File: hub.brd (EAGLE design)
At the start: 160 x 100 mm, 33 parts, among them U1 10118194-MICRO-USB, U2 LM3671MF-3.3/NOPBMF05A-M, U3 SN74LVC1T45DBVRDBV6-M, U4 SN74LVC1T45DBVRDBV6-M

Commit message: First draft complete?
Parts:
- removed JP3: I2C, pinhead:1X04
- removed LED2, LED3: (no value), led:CHIPLED_0805
- removed R7, R8: (no value), rcl:R0805
- removed U$7, U$8: KMR641NG, nebrius:KMR641NG
- added U$5: SSD1306-OLED, nebrius:SSD1306-OLED
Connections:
- removed net IO34: JP7.7, U$2.6
- removed net IO35: JP7.9, U$2.7
- removed net IO36: JP7.3, U$2.4
- removed net IO39: JP7.5, U$2.5
- removed net N$11: LED2.C, R7.2
- removed net N$13: LED3.C, R8.2
- removed net N$14: LED3.A, U$2.31
- removed net N$15: LED2.A, U$2.29
- new net IO19: JP7.2, U$2.31
- new net IO27: JP7.9, U$2.12
- new net IO33: JP7.3, U$2.9
- new net IO4: JP7.8, U$2.26
- net EN: no longer U$7.P$3
- net GND: now also U$5.2; no longer JP3.1, R7.1, R8.1, U$7.P$1, U$8.P$1
- net IO0: no longer U$8.P$3
- net IO16: now also JP7.4; no longer JP7.8
- net IO25: now also JP7.5; no longer JP7.2
- net IO26: now also JP7.7; no longer JP7.4
- net SCL: now also U$5.3; no longer JP3.4
- net SDA: now also U$5.4; no longer JP3.3
- net VCC: now also U$5.1; no longer JP3.2

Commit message: Polishing
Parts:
- R6: value 68 -> 220
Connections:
- net IO16 renamed GPIO16
- removed net IO17: JP7.6, U$2.28
- removed net IO19: JP7.2, U$2.31
- removed net IO25: JP7.5, U$2.10
- removed net IO26: JP7.7, U$2.11
- removed net IO27: JP7.9, U$2.12
- removed net IO33: JP7.3, U$2.9
- removed net IO4: JP7.8, U$2.26
- new net GPIO17: JP7.2, U$2.28
- new net GPIO25: JP7.7, U$2.10
- new net GPIO26: JP7.9, U$2.11
- new net GPIO27: JP7.8, U$2.12
- new net GPIO32: JP7.3, U$2.8
- new net GPIO33: JP7.5, U$2.9
- new net GPIO4: JP7.6, U$2.26
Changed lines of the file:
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@@
 <attribute name="VALUE" x="-82.296" y="-39.878" size="1.27" layer="27" ratio="10"/>
 </element>
-<element name="R6" library="rcl" library_urn="urn:adsk.eagle:library:334" package="R0805" package3d_urn="urn:adsk.eagle:package:23553/2" value="68" x="-80.01" y="-44.45" smashed="yes">
+<element name="R6" library="rcl" library_urn="urn:adsk.eagle:library:334" package="R0805" package3d_urn="urn:adsk.eagle:package:23553/2" value="220" x="-80.01" y="-44.45" smashed="yes">
 <attribute name="NAME" x="-80.645" y="-43.18" size="1.27" layer="25"/>
 <attribute name="POPULARITY" value="85" x="-80.01" y="-44.45" size="1.778" layer="27" display="off"/>
@@
 <wire x1="-79.06" y1="-44.45" x2="-86.36" y2="-42.13" width="0" layer="19" extent="1-1"/>
 </signal>
-<signal name="IO17">
-<contactref element="U$2" pad="28"/>
-<contactref element="JP7" pad="6"/>
-<wire x1="-104.53" y1="-48.26" x2="-115.57" y2="-60.96" width="0" layer="19" extent="1-1"/>
-</signal>
-<signal name="IO16">
+<signal name="GPIO16">
 <contactref element="U$2" pad="27"/>
 <contactref element="JP7" pad="4"/>
 <wire x1="-104.53" y1="-49.53" x2="-118.11" y2="-60.96" width="0" layer="19" extent="1-1"/>
 </signal>
-<signal name="IO25">
+<signal name="GPIO33">
+<contactref element="U$2" pad="9"/>
+<contactref element="JP7" pad="5"/>
+<wire x1="-121.53" y1="-45.72" x2="-115.57" y2="-63.5" width="0" layer="19" extent="1-1"/>
+</signal>
+<signal name="GPIO27">
+<contactref element="U$2" pad="12"/>
+<contactref element="JP7" pad="8"/>
+<wire x1="-121.53" y1="-49.53" x2="-113.03" y2="-60.96" width="0" layer="19" extent="1-1"/>
+</signal>
+<signal name="GPIO4">
+<contactref element="U$2" pad="26"/>
+<contactref element="JP7" pad="6"/>
+<wire x1="-104.53" y1="-50.8" x2="-115.57" y2="-60.96" width="0" layer="19" extent="1-1"/>
+</signal>
+<signal name="GPIO32">
+<contactref element="U$2" pad="8"/>
+<contactref element="JP7" pad="3"/>
+<wire x1="-121.53" y1="-44.45" x2="-118.11" y2="-63.5" width="0" layer="19" extent="1-1"/>
+</signal>
+<signal name="GPIO25">
 <contactref element="U$2" pad="10"/>
-<contactref element="JP7" pad="5"/>
-<wire x1="-121.53" y1="-46.99" x2="-115.57" y2="-63.5" width="0" layer="19" extent="1-1"/>
-</signal>
-<signal name="IO26">
+<contactref element="JP7" pad="7"/>
+<wire x1="-121.53" y1="-46.99" x2="-113.03" y2="-63.5" width="0" layer="19" extent="1-1"/>
+</signal>
+<signal name="GPIO26">
 <contactref element="U$2" pad="11"/>
-<contactref element="JP7" pad="7"/>
-<wire x1="-121.53" y1="-48.26" x2="-113.03" y2="-63.5" width="0" layer="19" extent="1-1"/>
-</signal>
-<signal name="IO33">
-<contactref element="U$2" pad="9"/>
-<contactref element="JP7" pad="3"/>
-<wire x1="-121.53" y1="-45.72" x2="-118.11" y2="-63.5" width="0" layer="19" extent="1-1"/>
-</signal>
-<signal name="IO27">
-<contactref element="U$2" pad="12"/>
 <contactref element="JP7" pad="9"/>
-<wire x1="-121.53" y1="-49.53" x2="-110.49" y2="-63.5" width="0" layer="19" extent="1-1"/>
-</signal>
-<signal name="IO4">
-<contactref element="U$2" pad="26"/>
-<contactref element="JP7" pad="8"/>
-<wire x1="-104.53" y1="-50.8" x2="-113.03" y2="-60.96" width="0" layer="19" extent="1-1"/>
-</signal>
-<signal name="IO19">
-<contactref element="U$2" pad="31"/>
+<wire x1="-121.53" y1="-48.26" x2="-110.49" y2="-63.5" width="0" layer="19" extent="1-1"/>
+</signal>
+<signal name="GPIO17">
+<contactref element="U$2" pad="28"/>
 <contactref element="JP7" pad="2"/>
-<wire x1="-104.53" y1="-44.45" x2="-120.65" y2="-60.96" width="0" layer="19" extent="1-1"/>
+<wire x1="-104.53" y1="-48.26" x2="-120.65" y2="-60.96" width="0" layer="19" extent="1-1"/>
 </signal>
 </signals>

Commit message: Tweaked and confirmed some connections
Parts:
- removed JP5: LED Type, jumper:JP2
- removed JP6: JTAG Enable, jumper:JP2
- added JP3: JTAG, pinhead:2X03
- JP1: value JTAG -> 3-pin LED strip; device pinhead:1X06 -> pinhead:1X03/90
- JP4: value LED Strip -> 4-pin LED Strip
- moved U$5 254.1 mm to (99.1, 54.6)
- moved JP7 245.7 mm to (102.9, 50.2)
- moved U$2 242.1 mm to (99.1, 81.3)
- moved JP4 197.7 mm to (118.7, 54.6), turned to 180 degrees
- moved JP1 187.1 mm to (117.5, 50.8), turned to 180 degrees
- moved S1 167.2 mm to (117.5, 67.9)
- moved U$3 151.1 mm to (85.1, 76.2), turned to 270 degrees
- moved U1 120.8 mm to (80.6, 64.8), turned to 270 degrees
- moved JP2 108.6 mm to (87.0, 51.4), turned to 180 degrees
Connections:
- removed net N$7: JP4.3, JP5.2
- removed net TRST_N: JP1.1, JP6.1
- net EN: now also JP3.1; no longer JP6.2, JP6.3
- net GND: now also JP1.1, JP3.6; no longer JP1.6, JP5.1
- net N$8: now also JP1.2, JP4.3; no longer JP4.2
- net N$9: now also JP4.2; no longer JP5.3
- net TCK: now also JP3.4; no longer JP1.4
- net TDI: now also JP3.3; no longer JP1.3
- net TDO: now also JP3.2; no longer JP1.2
- net TMS: now also JP3.5; no longer JP1.5
- net VCC: now also JP1.3

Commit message: More component arrangement
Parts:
- JP7: value (none) -> GPIO
- moved U$3 5.08 mm to (85.1, 71.1)
- moved U1 5.08 mm to (80.6, 59.7)
- moved JP3 0.64 mm to (118.1, 78.1), turned to 90 degrees
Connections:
- net GND: now also U1.M1, U1.M2, U1.M3, U1.M4
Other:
- outline, holes or cut-outs redrawn
- board text added: "EN"
- board text added: "GND"
- board text added: "Off"
- board text added: "TCK"
- board text added: "TDI"
- board text added: "TDO"
- board text added: "TMS"

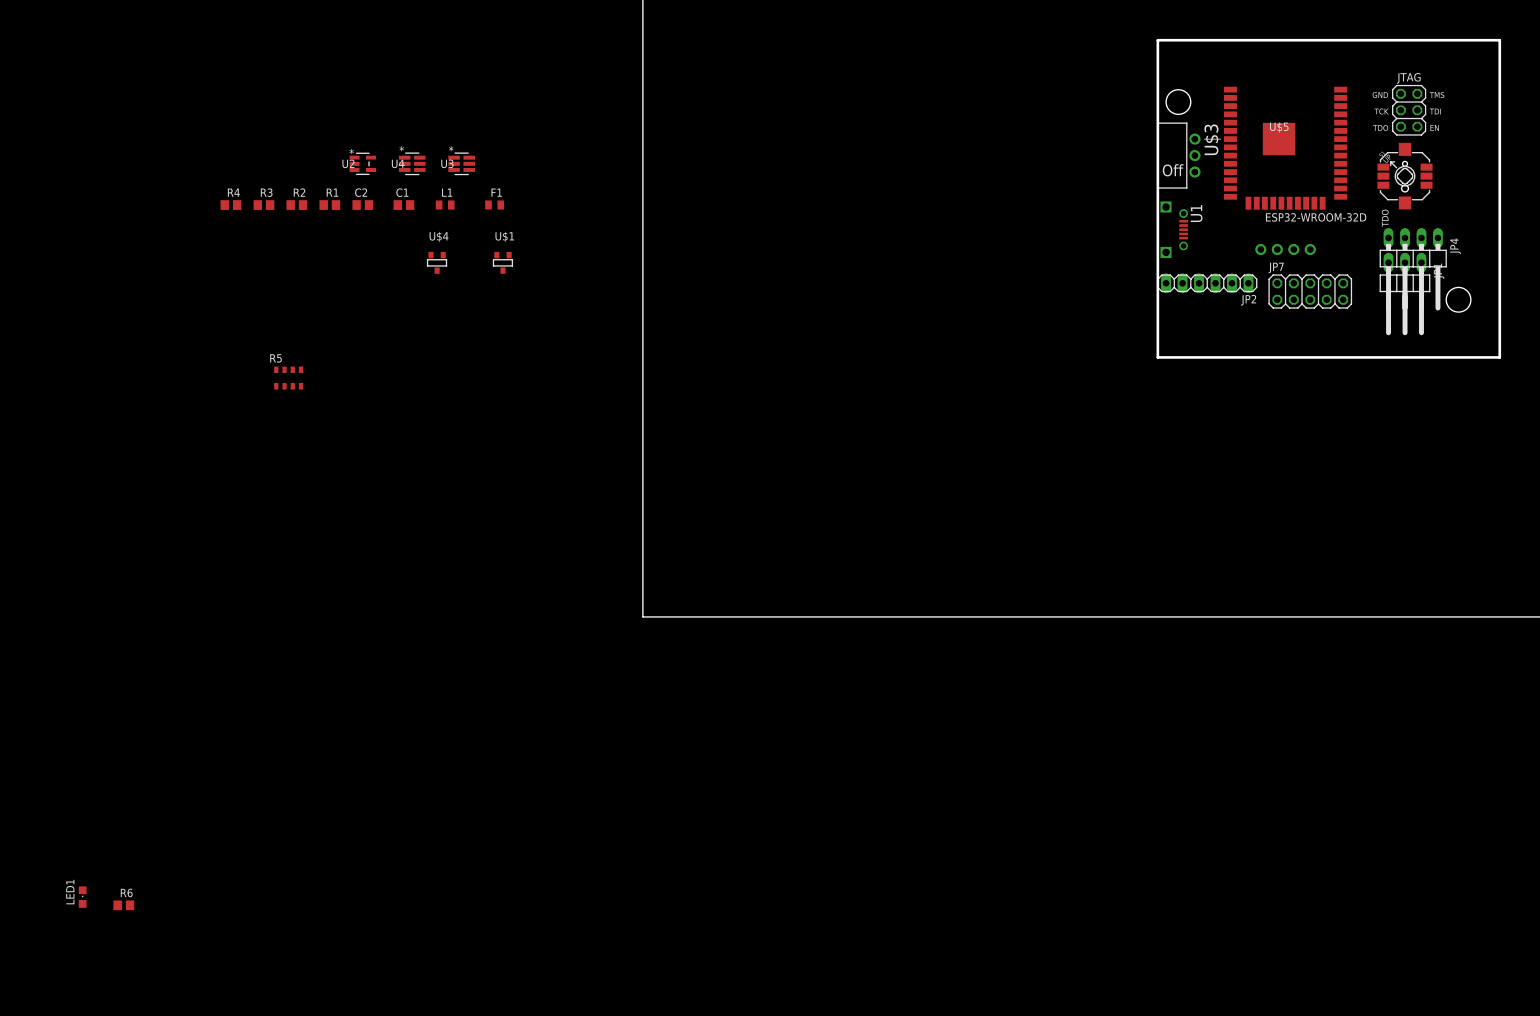
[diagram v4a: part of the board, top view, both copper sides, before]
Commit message: First draft of device placement
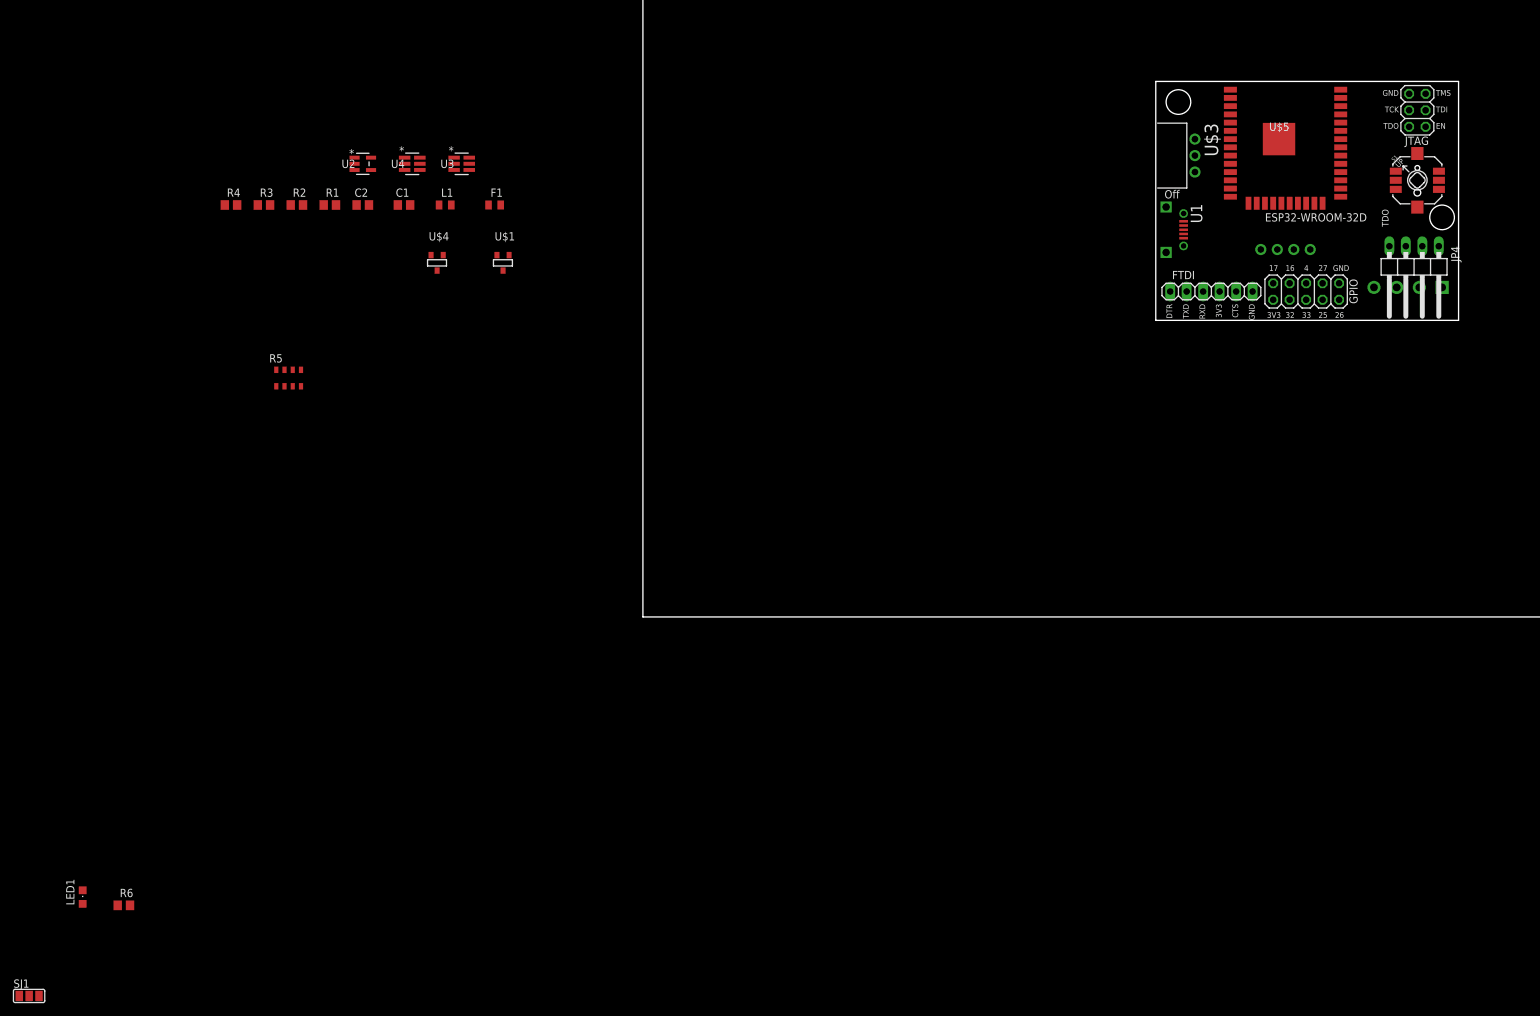
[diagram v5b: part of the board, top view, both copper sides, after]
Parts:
- removed JP1: 3-pin LED strip, pinhead:1X03/90
- added J1: (no value), SparkFun-Connectors:SCREWTERMINAL-3.5MM-4
- added SJ1: LED Type, jumper:SJ_2
- moved S1 2.01 mm to (119.4, 67.3)
- moved JP2 1.42 mm to (87.6, 50.2)
- moved JP4 1.28 mm to (118.9, 53.3)
- moved JP3 1.27 mm to (119.4, 78.1)
- moved JP7 0.64 mm to (102.2, 50.2)
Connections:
- new net N$7: J1.3, JP4.3, SJ1.2
- net GND: now also J1.4, SJ1.3; no longer JP1.1
- net N$8: now also SJ1.1; no longer JP1.2, JP4.3
- net N$9: now also J1.2
- net VCC: now also J1.1, JP2.3; no longer JP1.3
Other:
- outline, holes or cut-outs redrawn
- board text added: "16"
- board text added: "17"
- board text added: "25"
- board text added: "26"
- board text added: "27"
- board text added: "32"
- board text added: "33"
- board text added: "3V3"
- board text added: "4"
- board text added: "CTS"
- board text added: "DTR"
- board text added: "RXD"
- board text added: "TXD"

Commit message: First draft of component layout
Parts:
- removed JP4: 4-pin LED Strip, pinhead:1X04/90
- added JP1: (no value), pinhead:1X04
- moved SJ1 240.0 mm to (118.1, 52.7), flipped to the bottom
- moved J1 10.2 mm to (113.0, 49.5), flipped to the top
- moved U1 1.27 mm to (80.6, 58.4)
- moved JP7 0.64 mm to (102.9, 50.2)
- moved JP2 0.63 mm to (87.0, 50.2)
- moved S1 0.45 mm to (119.7, 67.6)
- moved JP3 0.32 mm to (119.4, 78.4)
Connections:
- net +5V: now also J1.1, JP1.1; no longer JP4.1
- net GND: now also JP1.4; no longer JP4.4
- net N$7: now also JP1.3; no longer JP4.3
- net N$9: now also JP1.2; no longer JP4.2
- net VCC: no longer J1.1
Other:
- outline, holes or cut-outs redrawn
- board text added: "3"
- board text added: "3-pin"
- board text added: "4-pin"
- board text added: "5V"
- board text added: "A"
- board text added: "B"
- board text added: "Clk"
- board text added: "Data"
